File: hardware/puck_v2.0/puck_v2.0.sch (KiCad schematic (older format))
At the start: 16 parts

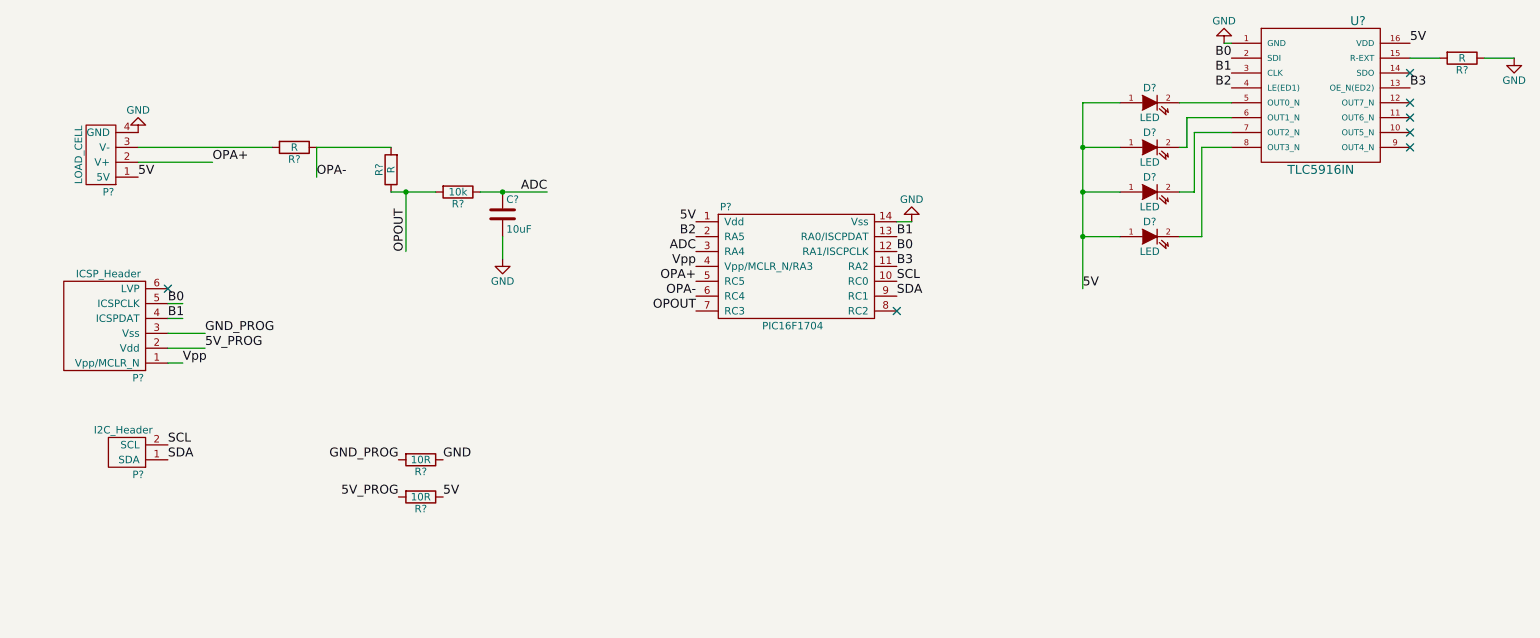
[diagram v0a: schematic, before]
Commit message: fixes working point of amplifier circuit in puck v2
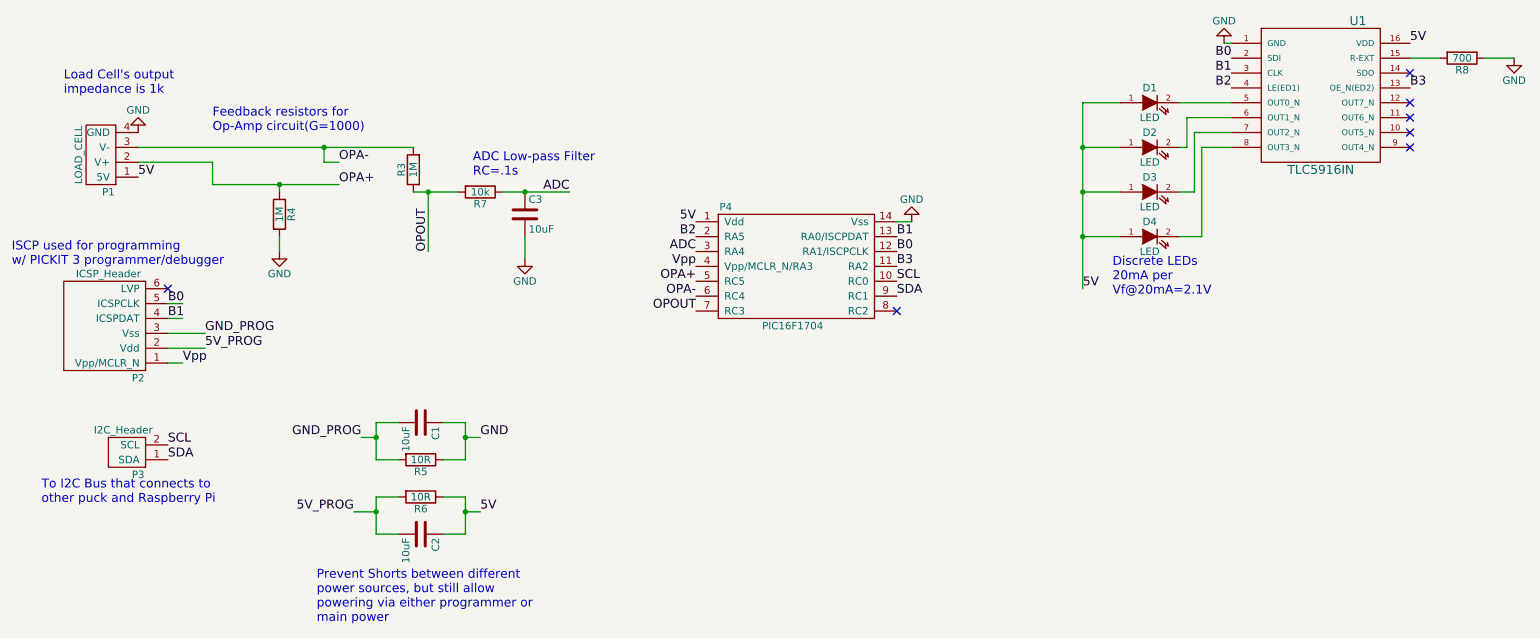
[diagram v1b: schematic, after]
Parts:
- removed R?: R, symbol R
- added C1, C2: 10uF, symbol C
- added R4: 1M, symbol R
- R3: renamed from R?; value R -> 1M
- R8: renamed from R?; value R -> 700
- gave numbers to parts that had none: 13
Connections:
- wire segments 32 -> 52
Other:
- note added: "ADC Low-pass Filter\nRC=.1s"
- note added: "Discrete LEDs\n20mA per\nVf@20mA=2.1V"
- note added: "Feedback resistors for\nOp-Amp circuit(G=1000)"
- note added: "ISCP used for programming \nw/ PICKIT 3 programmer/debugger"
- note added: "Load Cell's output \nimpedance is 1k"
- note added: "Prevent Shorts between different\npower sources, but still allow\npowering via either programmer or\nmain power"
- note added: "To I2C Bus that connects to\nother puck and Raspberry Pi"
- moved on the sheet: C3, R3, R7
